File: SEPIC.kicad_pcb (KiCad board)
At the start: 2 copper layers, 23 parts, among them J1 Screw_Terminal_01x02, J3 Screw_Terminal_01x02, J4 Conn_01x04_Male, J5 Conn_01x02_Male, J6 Conn_01x03_Male, J7 Screw_Terminal_01x02, U1 AP2205, U2 XL6009, U3 MCP48FVB21

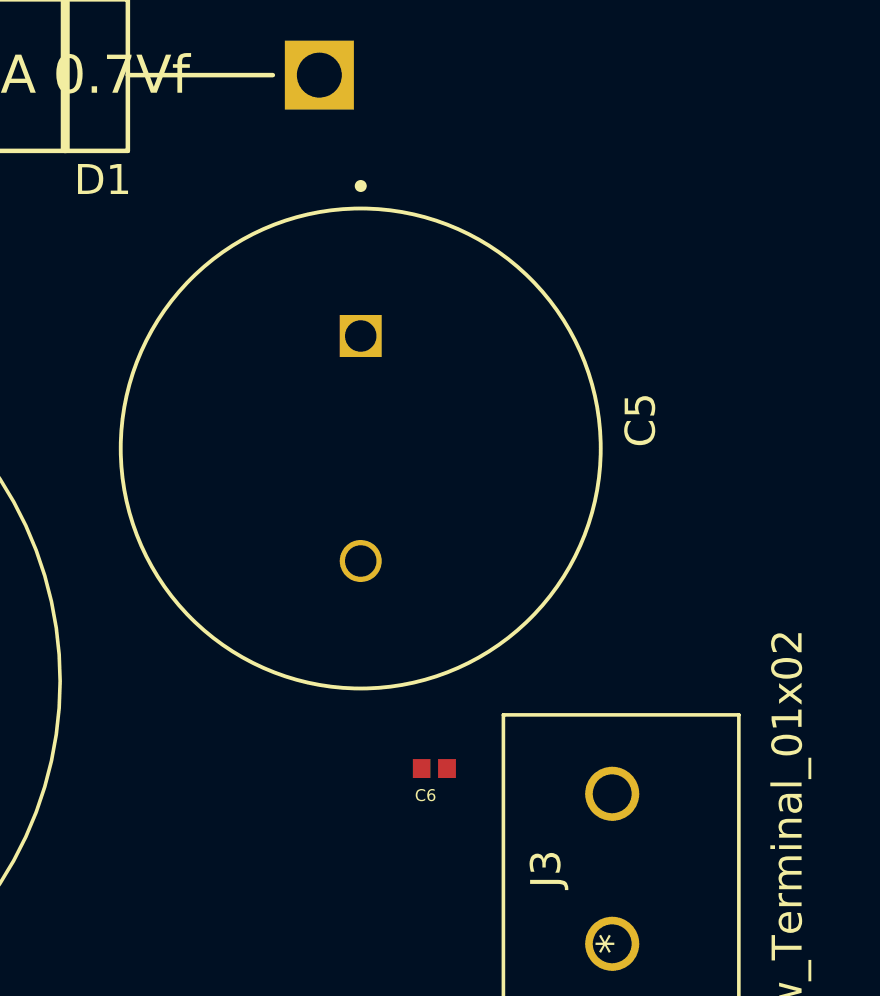
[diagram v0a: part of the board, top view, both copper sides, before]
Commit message: Rotated C5
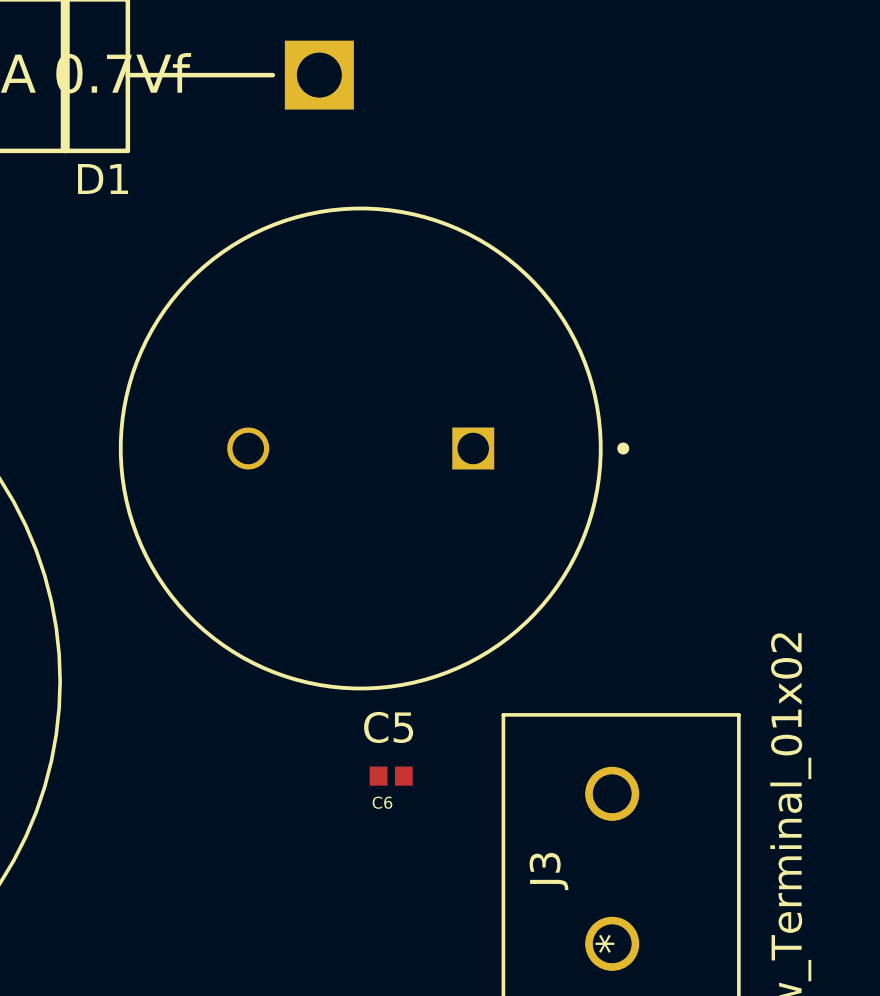
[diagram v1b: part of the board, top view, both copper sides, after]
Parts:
- moved C6 1.46 mm to (194.3, 77.2)
- turned C5 to 180 degrees
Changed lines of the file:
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@@
   )
   (module Footprints:EEU-FC1J471 (layer F.Cu)
-    (at 193.294 66.294 270)
-    (fp_text reference C5 (at -0.95 -9.335 90) (layer F.SilkS)
+    (at 193.294 66.294 180)
+    (fp_text reference C5 (at -0.95 -9.335) (layer F.SilkS)
       (effects (font (size 1 1) (thickness 0.15)))
     )
-    (fp_text value "470µF 63V 1.765A" (at 0 10.16 90) (layer F.Fab)
+    (fp_text value "470µF 63V 1.765A" (at 0 10.16) (layer F.Fab)
       (effects (font (size 1 1) (thickness 0.15)))
     )
@@
     (fp_circle (center 0 0) (end 8 0) (layer F.SilkS) (width 0.127))
     (fp_circle (center 0 0) (end 8 0) (layer F.Fab) (width 0.127))
-    (pad 1 thru_hole rect (at -3.75 0 270) (size 1.4 1.4) (drill 1.05) (layers *.Cu *.Mask)
+    (pad 1 thru_hole rect (at -3.75 0 180) (size 1.4 1.4) (drill 1.05) (layers *.Cu *.Mask)
       (net 4 /VOUT))
-    (pad 2 thru_hole circle (at 3.75 0 270) (size 1.4 1.4) (drill 1.05) (layers *.Cu *.Mask)
+    (pad 2 thru_hole circle (at 3.75 0 180) (size 1.4 1.4) (drill 1.05) (layers *.Cu *.Mask)
       (net 2 GND))
   )
   (module Footprints:04025C102KAT2A (layer F.Cu)
-    (at 195.746 76.962 180)
+    (at 194.31 77.216 180)
     (fp_text reference C6 (at 0.29 -0.9) (layer F.SilkS)
       (effects (font (size 0.393701 0.393701) (thickness 0.15)))

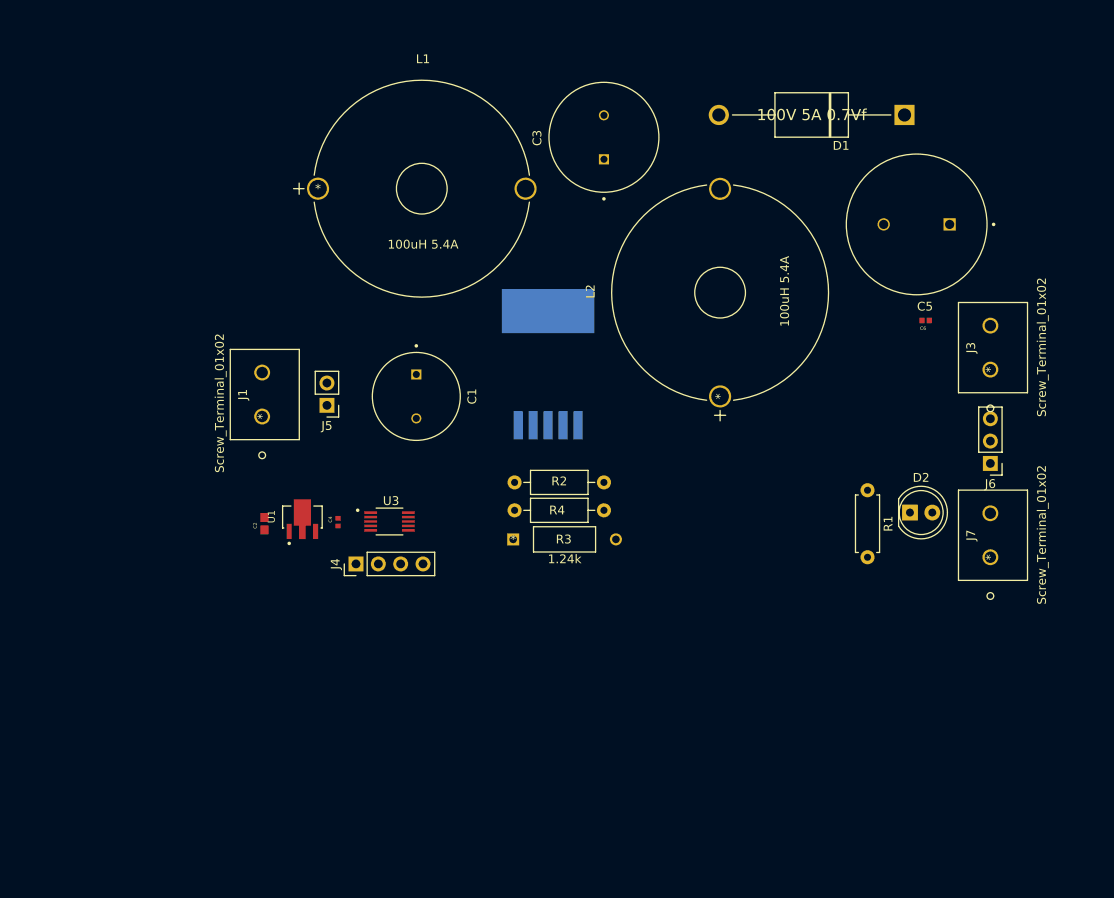
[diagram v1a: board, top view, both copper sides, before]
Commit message: Added cut line
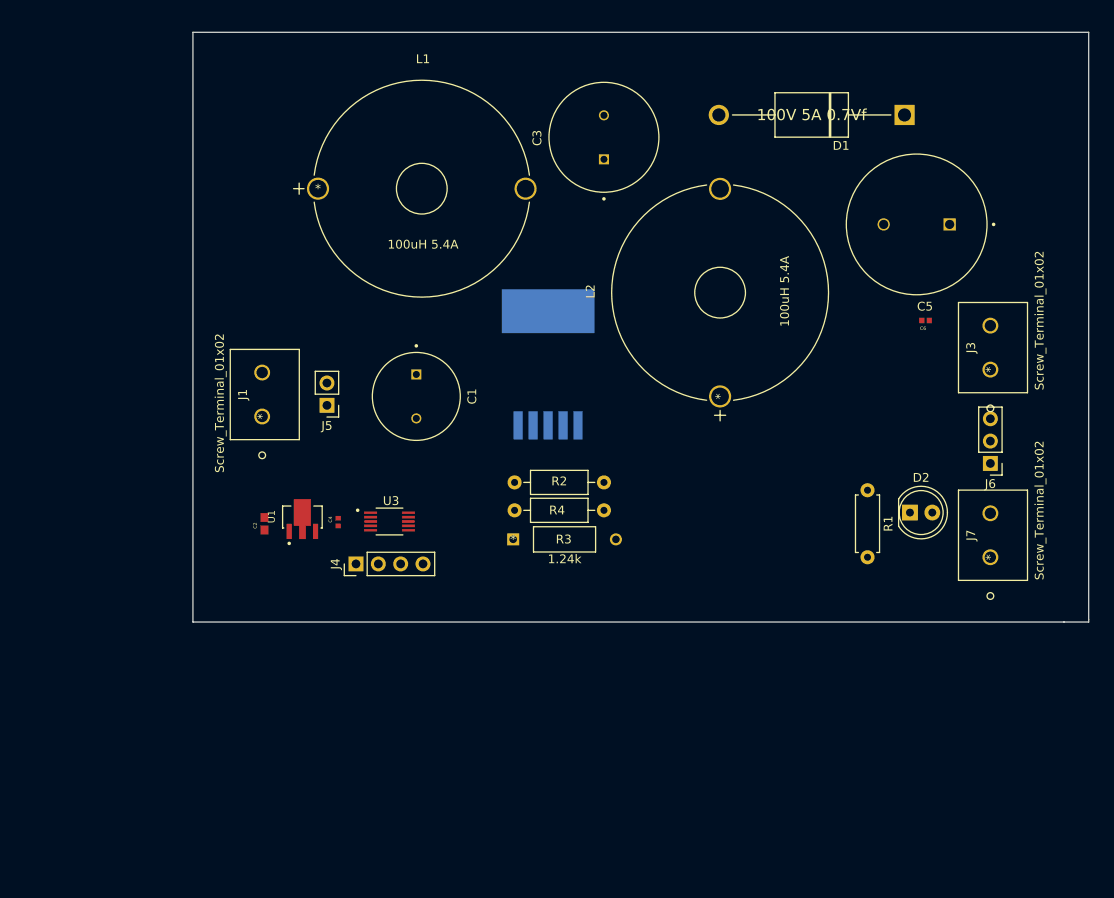
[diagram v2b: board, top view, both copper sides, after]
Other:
- board outline added: 101.9 x 67.1 mm
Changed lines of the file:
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@@
   (general
     (thickness 1.6)
-    (drawings 0)
+    (drawings 6)
     (tracks 0)
     (zones 0)
@@
     (46 B.CrtYd user)
     (47 F.CrtYd user)
-    (48 B.Fab user)
+    (48 B.Fab user hide)
     (49 F.Fab user hide)
   )
@@
       (effects (font (size 1 1) (thickness 0.15)))
     )
-    (fp_text value Screw_Terminal_01x02 (at 2.55 5.85 90) (layer F.SilkS)
+    (fp_text value Screw_Terminal_01x02 (at 5.588 5.588 90) (layer F.SilkS)
       (effects (font (size 1 1) (thickness 0.15)))
     )
@@
       (effects (font (size 1 1) (thickness 0.15)))
     )
-    (fp_text value Screw_Terminal_01x02 (at 2.55 5.85 90) (layer F.SilkS)
+    (fp_text value Screw_Terminal_01x02 (at 5.334 5.588 90) (layer F.SilkS)
       (effects (font (size 1 1) (thickness 0.15)))
     )
@@
       (net 11 "Net-(C3-Pad2)"))
   )
+  (gr_line (start 212.852 111.506) (end 210.058 111.506) (layer Edge.Cuts) (width 0.05))
+  (gr_line (start 212.852 111.252) (end 212.852 111.506) (layer Edge.Cuts) (width 0.05))
+  (gr_line (start 212.852 44.45) (end 212.852 111.252) (layer Edge.Cuts) (width 0.05))
+  (gr_line (start 110.998 44.45) (end 212.852 44.45) (layer Edge.Cuts) (width 0.05))
+  (gr_line (start 110.998 111.506) (end 110.998 44.45) (layer Edge.Cuts) (width 0.05))
+  (gr_line (start 210.058 111.506) (end 110.998 111.506) (layer Edge.Cuts) (width 0.05))
 )

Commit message: Mostly done
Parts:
- moved D1 5.08 mm to (186.4, 53.8)
- moved L1 3.10 mm to (134.6, 64.0)
- moved J5 2.62 mm to (128.5, 85.6), turned to 270 degrees
- moved U3 2.03 mm to (133.3, 98.0), turned to 270 degrees
- moved C6 1.61 mm to (192.8, 77.7)
- moved C1 0.80 mm to (137.2, 85.6)
- moved C2 0.25 mm to (119.1, 100.6)
- turned C3 to 45 degrees
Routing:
- net +3V3: track 0.00 -> 161.2 mm, vias 0 -> 3
- net VCC: track 0.00 -> 109.0 mm
- net GND: track 0.00 -> 83.0 mm, vias 0 -> 35
- net /VOUT: track 0.00 -> 47.5 mm
- net Net-(C3-Pad1): track 0.00 -> 27.5 mm
- net Net-(R4-Pad1): track 0.00 -> 27.3 mm, vias 0 -> 2
- net Net-(C3-Pad2): track 0.00 -> 25.0 mm
- net Net-(R2-Pad2): track 0.00 -> 13.2 mm
- net CS: track 0.00 -> 10.4 mm
- net SCK: track 0.00 -> 8.92 mm
- net SDO: track 0.00 -> 6.29 mm
- net Net-(D2-Pad1): track 0.00 -> 5.88 mm
- net SDI: track 0.00 -> 5.65 mm
- added copper zone on B.Cu, net /VOUT
- added copper zone on F.Cu, net /VOUT
- added copper zone on B.Cu, net GND
- added copper zone on F.Cu, net GND
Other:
- board text added: "+"
- board text added: "3V3"
- board text added: "CS"
- board text added: "GND"
- board text added: "SCK"
- board text added: "SDI"
- board text added: "SDO"
- board text added: "SPI SEPIC v0.1 License: CC BY 4.0"
- board text added: "See MCP48FVB21-E/UN datasheet for SPI interface"
- board text added: "VIN"
- board text added: "VOUT"

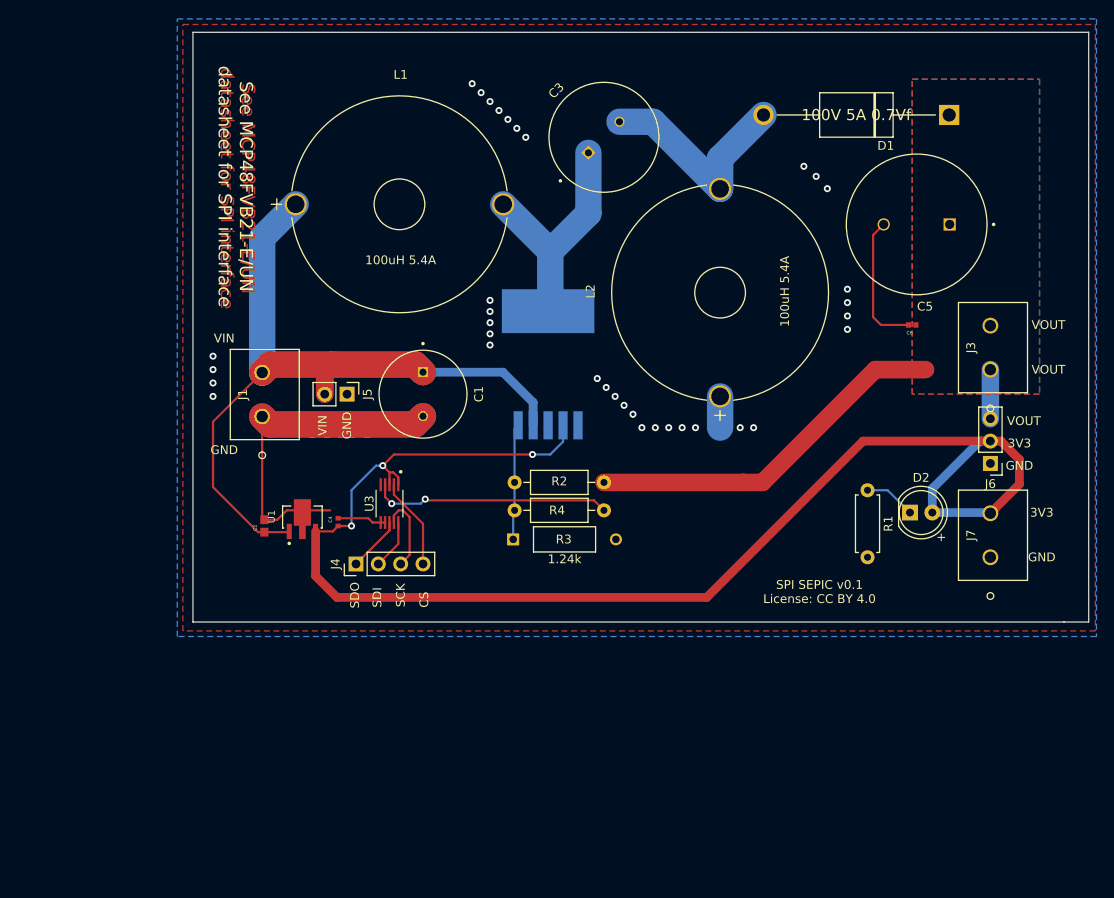
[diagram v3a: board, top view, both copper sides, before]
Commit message: Added some optional capacitors
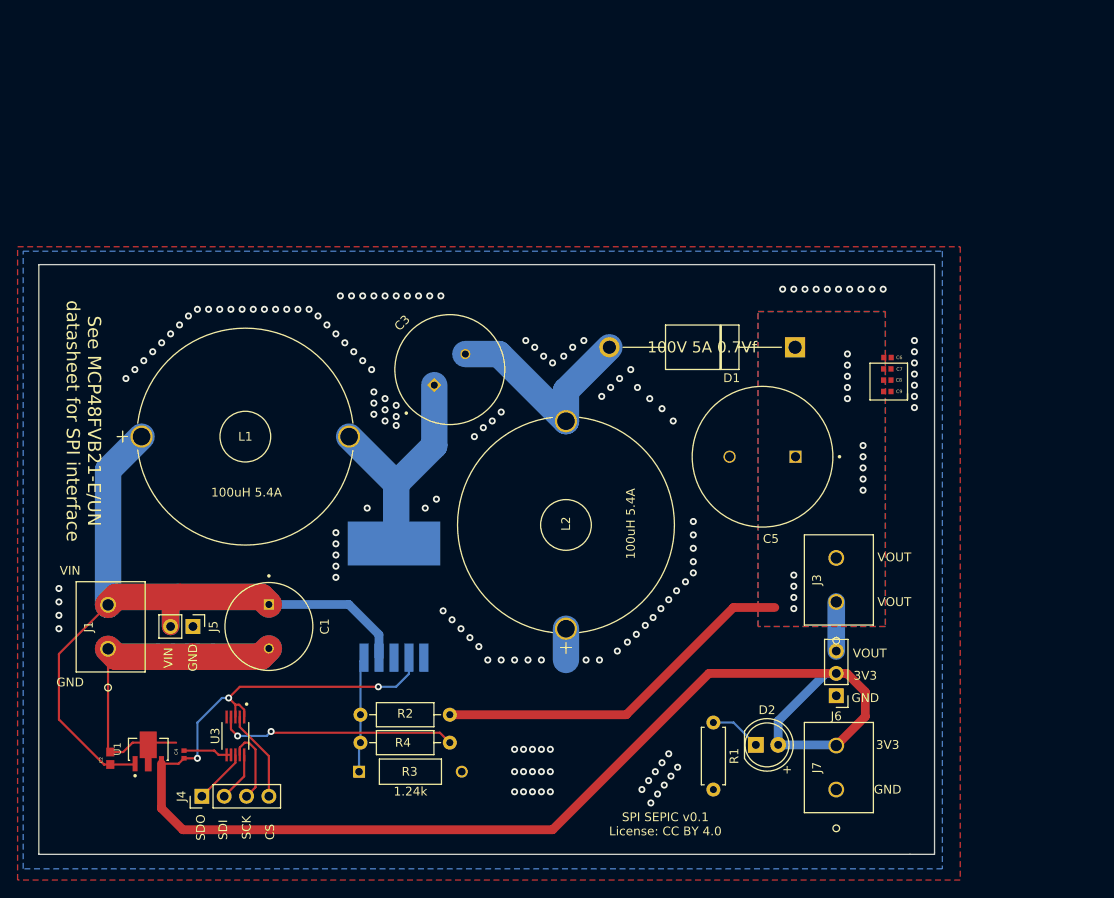
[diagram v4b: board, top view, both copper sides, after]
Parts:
- added C7: 1000pF, Footprints:04025C102KAT2A, F.Cu at (190.0, 82.7)
- added C8: 1000pF, Footprints:04025C102KAT2A, F.Cu at (190.0, 84.0)
- added C9: 1000pF, Footprints:04025C102KAT2A, F.Cu at (190.0, 85.3)
- moved L1 31.7 mm to (117.1, 90.4)
- moved C3 31.7 mm to (140.2, 82.8)
- moved C2 31.7 mm to (101.6, 127.0)
- moved C5 31.7 mm to (175.8, 92.7)
- moved D1 31.7 mm to (168.9, 80.3)
- moved D2 31.7 mm to (175.0, 125.5)
- moved J4 31.7 mm to (112.0, 131.3)
- moved L2 31.7 mm to (153.4, 100.3)
- moved R2 31.7 mm to (140.2, 122.0)
- moved R3 31.7 mm to (135.6, 128.5)
- moved R4 31.7 mm to (140.2, 125.2)
- moved J6 31.7 mm to (184.2, 119.9)
- moved J7 31.7 mm to (184.2, 130.6)
- moved R1 31.7 mm to (170.2, 122.9)
- moved C1 31.7 mm to (119.6, 112.0)
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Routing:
- net GND: track 83.0 -> 67.6 mm, vias 35 -> 144
- net /VOUT: track 47.5 -> 47.6 mm, vias 0 -> 14
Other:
- board text added: "I_OUT = 4 / 1.2 / (1 + (V_OUT + V_D) / V_IN)"

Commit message: Added mounting hole
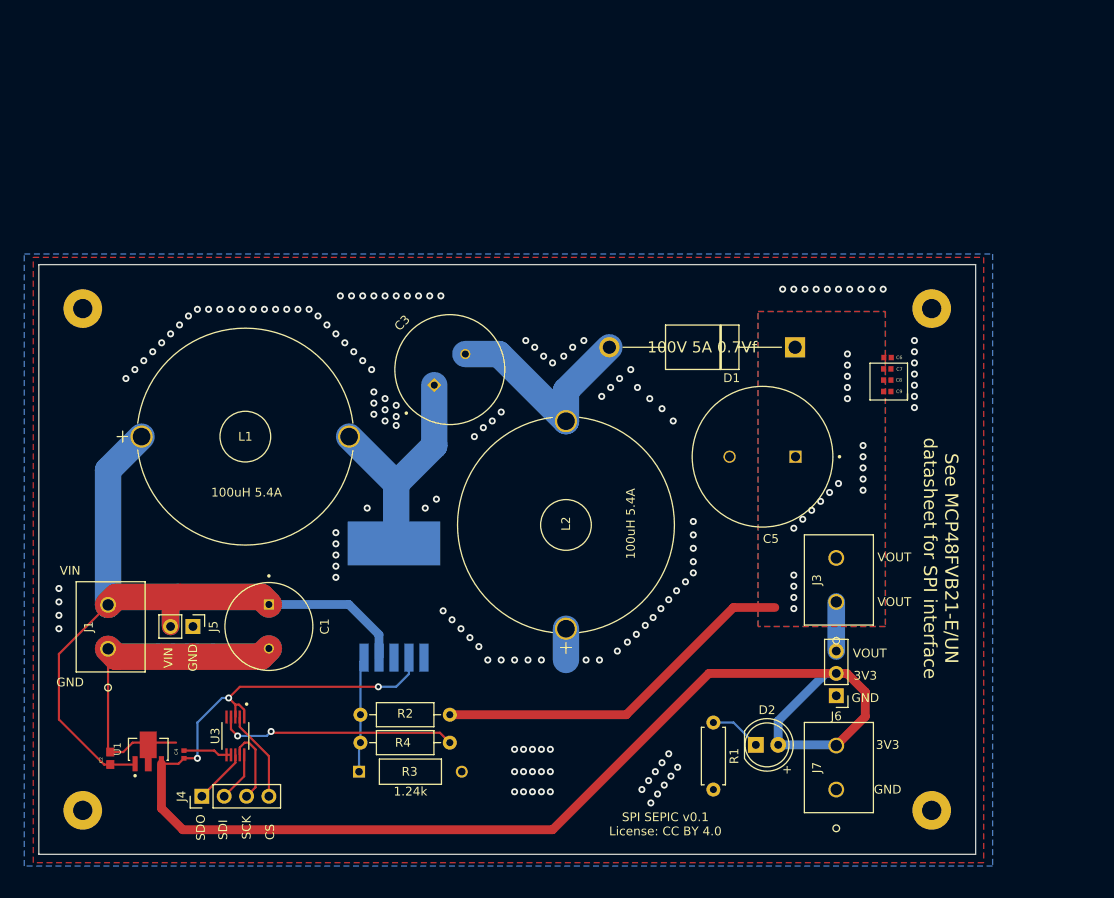
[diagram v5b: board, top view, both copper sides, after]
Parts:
- added REF**: MountingHole_2.2mm_M2_Pad, MountingHole:MountingHole_2.2mm_M2_Pad, F.Cu at (195.0, 132.9)
- added REF**: MountingHole_2.2mm_M2_Pad, MountingHole:MountingHole_2.2mm_M2_Pad, F.Cu at (195.0, 75.9)
- added REF**: MountingHole_2.2mm_M2_Pad, MountingHole:MountingHole_2.2mm_M2_Pad, F.Cu at (98.5, 75.9)
- added REF**: MountingHole_2.2mm_M2_Pad, MountingHole:MountingHole_2.2mm_M2_Pad, F.Cu at (98.5, 132.9)
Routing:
- net /VOUT: vias 14 -> 20
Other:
- board size 101.9 x 67.1 mm -> 106.5 x 67.1 mm
